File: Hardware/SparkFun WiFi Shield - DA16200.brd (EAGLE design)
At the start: 59.7 x 53.3 mm, 131 parts, among them J1 CORTEX_JTAG_DEBUG, U1 DA16200MOD-AAC4WA32

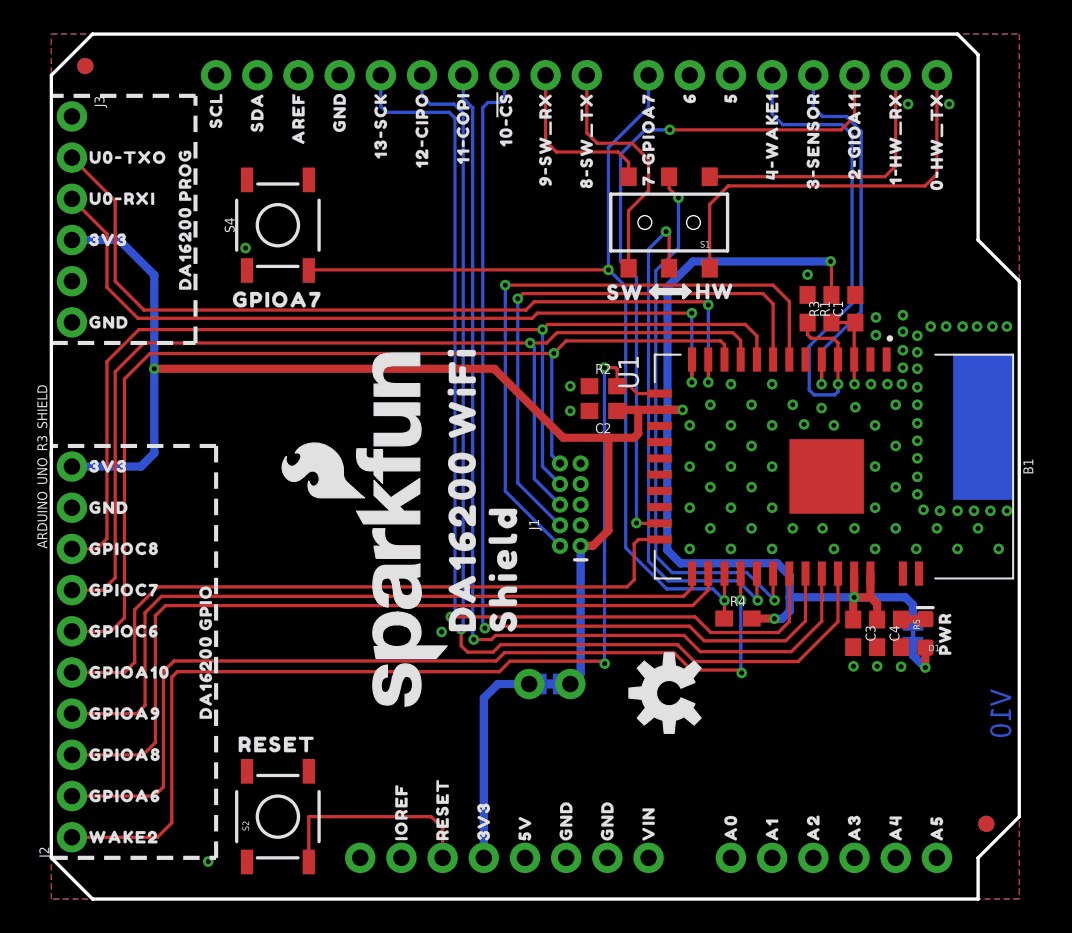
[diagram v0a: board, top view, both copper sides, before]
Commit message: V10 Dialog Changes
- GPIOA6 needs 4.7k Pullup
- GPIOA10 - added 2-way jumper for MCU (SPI Interrupt) and Header (PWM)
- GPIOC6,7,8 not needed for JTAG
- Removed RTC Sensor, RTC_WAKE1, RTC_WAKE2
- PCB - Moved VDD trace, enlarged ground connection for RF GND on bottom, added more vias in large ground areas
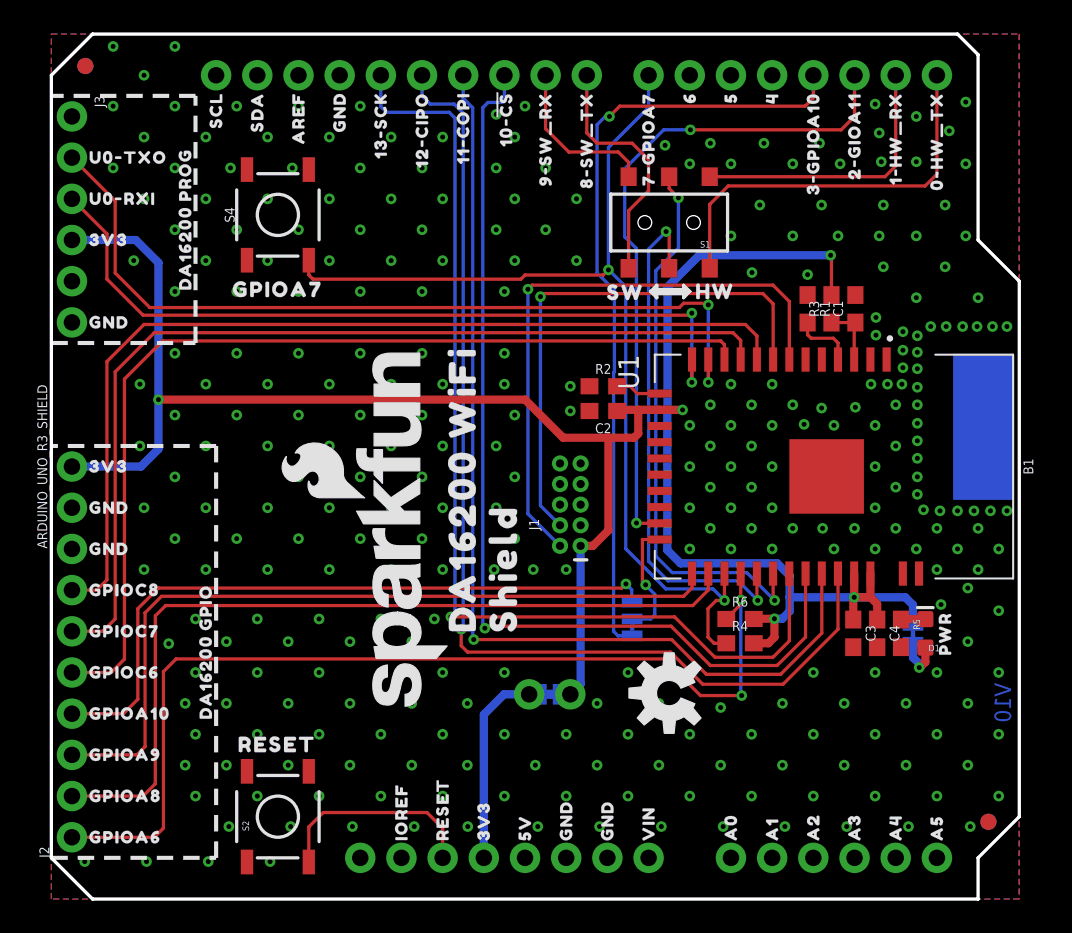
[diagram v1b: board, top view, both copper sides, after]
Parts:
- removed U$69: (no value), output:4#WAKE10
- removed U$96: (no value), output:WAKE20
- added JP2: (no value), SparkFun-Jumpers:SMT-JUMPER_3_1-NC_TRACE_NO-SILK
- added R6: 4.7k, SparkFun-Resistors:0603
- added U$35: (no value), output:GND0
- added U$51: (no value), output:3#GPIOA100
- U$18: device output:4#WAKE10 -> output:40
- U$23: device output:3#SENSOR0 -> output:40
- U$50: device output:WAKE20 -> output:GND0
- U$68: device output:3#SENSOR0 -> output:3#GPIOA100
- moved U$50 17.8 mm to (1.78, 21.6)
- moved U$46 2.54 mm to (1.78, 14.0)
- moved U$47 2.54 mm to (1.78, 11.4)
- moved U$49 2.54 mm to (1.78, 6.35)
- moved U$91 2.54 mm to (1.78, 14.0)
- moved U$92 2.54 mm to (1.78, 11.4)
- moved U$94 2.54 mm to (1.78, 6.35)
- moved U$17 2.54 mm to (1.78, 3.81)
- moved U$95 2.54 mm to (1.78, 3.81)
- moved U$23 2.54 mm to (44.5, 50.3), flipped to the bottom
- moved U$44 2.54 mm to (1.78, 19.1)
- moved U$45 2.54 mm to (1.78, 16.5)
- moved U$48 2.54 mm to (1.78, 8.89)
- moved U$89 2.54 mm to (1.78, 19.1)
- moved U$90 2.54 mm to (1.78, 16.5)
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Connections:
- removed net GPIOA6: J2.2, U1.27
- removed net GPIOA8: J2.3, U1.25
- removed net GPIOA9: J2.4, U1.24
- removed net GPIOC6: J1.10, J2.6, U1.11
- removed net GPIOC7: J1.6, J2.7, U1.10
- removed net GPIOC8: J1.8, J2.8, U1.9
- removed net RTC_SENSOR: B1.D3, U1.5
- removed net RTC_WAKE2: J2.1, R2.2, U1.14
- new net ARD_GPIOA10: B1.D3, JP2.3
- new net HEADER_GPIOA10: J2.4, JP2.1
- new net HEADER_GPIOA6: J2.1, R6.1, U1.27
- new net HEADER_GPIOA8: J2.2, U1.25
- new net HEADER_GPIOA9: J2.3, U1.24
- new net HEADER_GPIOC6: J2.5, U1.11
- new net HEADER_GPIOC7: J2.6, U1.10
- new net HEADER_GPIOC8: J2.7, U1.9
- new net HEADER_RTC_WAKE2: R2.2, U1.14
- net 3.3V: now also R6.2
- net GND: now also J2.8
- net GPIOA10: now also JP2.2; no longer J2.5
- net RTC_WAKE1: no longer B1.D4
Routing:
- net GPIOC7: track 67.4 -> 0.00 mm, vias 1 -> 0
- net GPIOC8: track 66.1 -> 0.00 mm, vias 1 -> 0
- net RTC_WAKE2: track 65.6 -> 0.00 mm, vias 2 -> 0
- net GPIOC6: track 64.4 -> 0.00 mm, vias 1 -> 0
- net HEADER_GPIOA6: track 0.00 -> 61.6 mm, vias 0 -> 2
- net HEADER_GPIOC6: track 0.00 -> 59.8 mm
- net HEADER_GPIOC7: track 0.00 -> 59.2 mm
- net HEADER_GPIOC8: track 0.00 -> 58.7 mm
- net GPIOA6: track 55.8 -> 0.00 mm, vias 2 -> 0
- net HEADER_GPIOA8: track 0.00 -> 51.6 mm
- net GPIOA8: track 49.0 -> 0.00 mm
- net ARD_GPIOA10: track 0.00 -> 48.4 mm, vias 0 -> 1
- net HEADER_GPIOA9: track 0.00 -> 48.2 mm
- net GPIOA9: track 45.7 -> 0.00 mm
- net HEADER_GPIOA10: track 0.00 -> 42.0 mm, vias 0 -> 1
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
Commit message: Parts Update
Updated library for module, added 470k resistor, updated symbols, added jumper notes
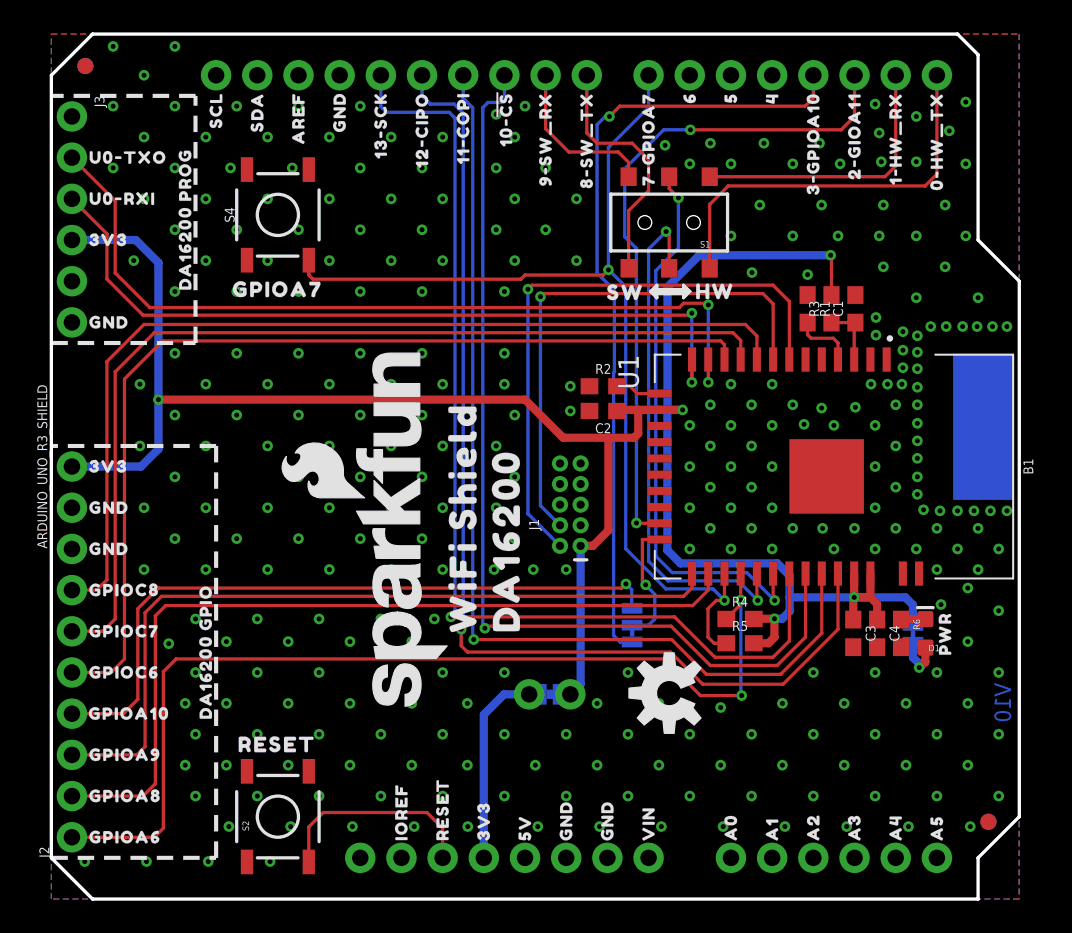
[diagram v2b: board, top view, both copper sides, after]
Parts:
- removed U$102: (no value), output:DA16200_WIFI0
- removed U$103: (no value), output:SHIELD0
- added U$106: (no value), output:HEADER0
- added U$107: (no value), output:WIFI_SHIELD0
- added U$108: (no value), output:DA162000
- added U$69: (no value), output:GPIOA100
- added U$96: (no value), output:D30
- C1: value 1.0uF -> 1uF
- JP2: device SparkFun-Jumpers:SMT-JUMPER_3_1-NC_TRACE_NO-SILK -> SparkFun-Jumpers:SMT-JUMPER_3_1-NC_TRACE_SILK
- R5: value 200 -> 4.7k
- R6: value 4.7k -> 200
- S1: device SparkFun-Electromechanical:AYZ0202 -> SparkFun-Switches:SWITCH_DPDT_SMD_AYZ0202
- U$100: device output:DA16200_WIFI0 -> output:WIFI_SHIELD0
- U$101: device output:SHIELD0 -> output:DA162000
- U1: value DA16200MOD-AAC4WA32 -> DA16200MOD; device DA16200MOD-AAC4WA32:XCVR_DA16200MOD-AAC4WA32 -> DA16200MOD:XCVR_DA16200MOD-AAC4WA32
- moved U$101 27.5 mm to (14.0, 38.2), flipped to the bottom, turned to 180 degrees
- moved U$100 23.9 mm to (14.0, 35.6), flipped to the bottom, turned to 180 degrees
- moved R6 9.97 mm to (52.4, 16.4), turned to 270 degrees
- moved R5 9.95 mm to (42.5, 15.8), turned to 0 degrees
- moved U$47 6.10 mm to (7.87, 11.4)
- moved U$92 6.10 mm to (7.87, 11.4)
- moved R4 1.50 mm to (42.5, 17.3)
- moved JP2 0.38 mm to (35.8, 16.9)
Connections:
- net 3.3V: now also R5.2; no longer R6.2
- net GND: now also R6.2; no longer R5.2
- net GPIOA7: now also R5.1; no longer R4.1
- net HEADER_GPIOA6: now also R4.1; no longer R6.1
- net N$5: now also R6.1; no longer R5.1

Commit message: Added I2C
Added I2C connections, Qwiic connector, pullup resistors, and jumper
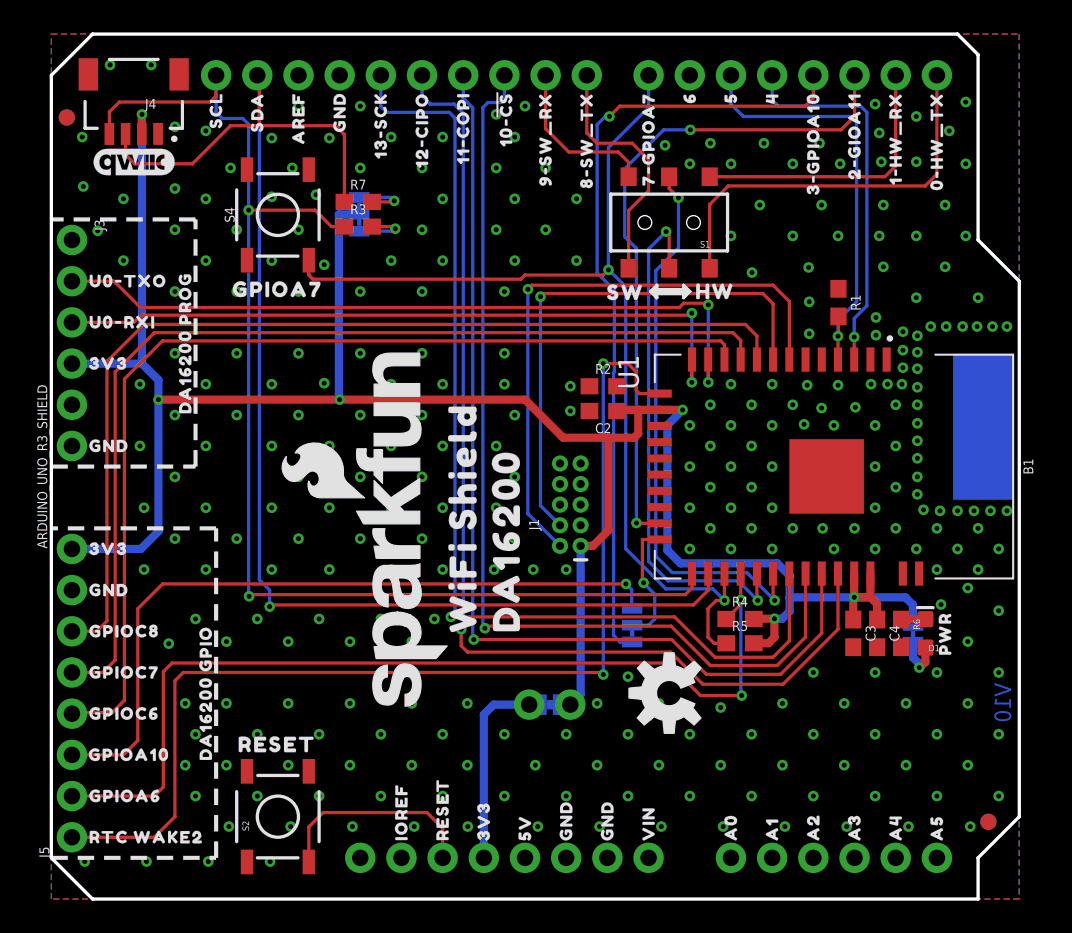
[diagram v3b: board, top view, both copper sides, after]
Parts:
- removed C1: 1uF, SparkFun-Capacitors:0603
- removed J2: (no value), SparkFun-Connectors:1X10_NO_SILK
- removed U$50: (no value), output:GND0
- removed U$93: (no value), output:GPIOA90
- removed U$94: (no value), output:GPIOA80
- added J4: QWIIC_RIGHT_ANGLE, SparkFun-Connectors:JST04_1MM_RA
- added J5: (no value), SparkFun-Connectors:1X08_NO_SILK
- added JP3: (no value), SparkFun-Jumpers:SMT-JUMPER_3_2-NC_TRACE_SILK
- added LOGO4: QWIIC_LOGO_5MM, SparkFun-Aesthetics:QWIIC_5MM
- added R7: 4.7k, SparkFun-Resistors:0603
- R3: value 470k -> 4.7k
- U$35: device output:GND0 -> output:RTC_WAKE20
- U$48: device output:GPIOA90 -> output:RTC_WAKE20
- U$49: device output:GPIOA80 -> output:#I2C#0
- moved U$49 39.0 mm to (17.3, 42.2), flipped to the bottom, turned to 90 degrees
- moved R3 29.6 mm to (18.9, 41.5), turned to 0 degrees
- moved U$35 17.8 mm to (1.78, 3.81), flipped to the top, turned to 0 degrees
- moved U$52 7.62 mm to (1.78, 27.9)
- moved U$86 7.62 mm to (1.78, 27.9)
- moved J3 7.62 mm to (1.27, 40.6)
- moved U$105 7.62 mm to (8.26, 34.3)
- moved U$37 7.62 mm to (1.78, 33.0)
- moved U$53 7.62 mm to (1.78, 38.1)
- moved U$54 7.62 mm to (1.78, 35.6)
- moved U$83 7.62 mm to (1.78, 38.1)
- moved U$84 7.62 mm to (1.78, 35.6)
- moved U$85 7.62 mm to (1.78, 33.0)
- moved U$41 5.08 mm to (1.78, 21.6)
- moved U$87 5.08 mm to (1.78, 21.6)
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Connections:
- removed net HEADER_GPIOA8: J2.2, U1.25
- removed net HEADER_GPIOA9: J2.3, U1.24
- new net ARD_SCL: B1.SCL, J4.4, R3.1, U1.24
- new net ARD_SDA: B1.SDA, J4.3, R7.1, U1.25
- new net N$3: JP3.3, R3.2
- new net N$4: JP3.1, R7.2
- net 3.3V: now also J4.2, J5.8, JP3.2; no longer J2.10, R3.2
- net GND: now also J4.1, J5.7; no longer C1.2, J2.8, J2.9
- net HEADER_GPIOA10: now also J5.3; no longer J2.4
- net HEADER_GPIOA6: now also J5.2; no longer J2.1
- net HEADER_GPIOC6: now also J5.4; no longer J2.5
- net HEADER_GPIOC7: now also J5.5; no longer J2.6
- net HEADER_GPIOC8: now also J5.6; no longer J2.7
- net HEADER_RTC_WAKE2: now also J5.1
- net RTC_PWR_KEY: now also B1.D4; no longer C1.1, R3.1
- net RTC_WAKE1: now also B1.D5
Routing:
- net ARD_SDA: track 0.00 -> 85.2 mm, vias 0 -> 1
- net ARD_SCL: track 0.00 -> 78.1 mm, vias 0 -> 2
- net HEADER_RTC_WAKE2: track 2.81 -> 67.2 mm, vias 0 -> 2
- net HEADER_GPIOA8: track 51.6 -> 0.00 mm
- net HEADER_GPIOA9: track 48.2 -> 0.00 mm
- net RTC_WAKE1: track 3.86 -> 26.3 mm, vias 0 -> 1
- net RTC_PWR_KEY: track 3.82 -> 23.2 mm, vias 0 -> 1
- net 3.3V: track 139.2 -> 145.4 mm, vias 5 -> 6
- net U0TXO: track 52.0 -> 46.3 mm
- net U0RXI: track 48.6 -> 44.1 mm
- net N$3: track 0.00 -> 3.77 mm, vias 0 -> 1
- net N$4: track 0.00 -> 3.65 mm, vias 0 -> 1
- net HEADER_GPIOA6: track 61.6 -> 58.8 mm
- net HEADER_GPIOC6: track 59.8 -> 62.4 mm
- net HEADER_GPIOC8: track 58.7 -> 61.2 mm
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
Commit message: V10 Design Review Changes
Updated label positions, added notes to sch
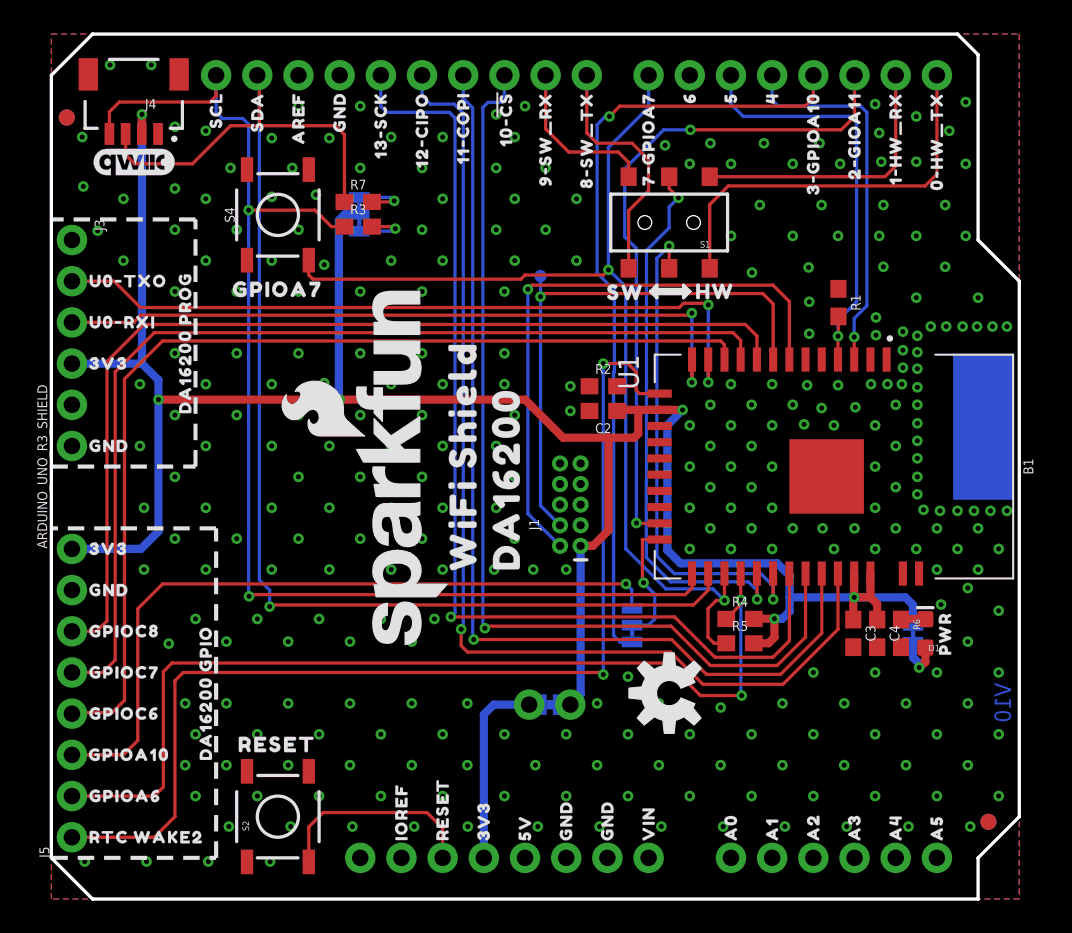
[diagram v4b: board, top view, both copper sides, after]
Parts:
- added TP1: (no value), SparkFun-Connectors:PAD.03X.03
- J4: value QWIIC_RIGHT_ANGLE -> QWIIC_RA
- moved LOGO3 7.73 mm to (19.1, 24.1)
- moved U$100 7.62 mm to (14.0, 27.9)
- moved U$101 7.62 mm to (14.0, 30.6)
- moved LOGO1 3.81 mm to (21.6, 26.7)
- moved U$107 3.81 mm to (25.4, 19.1)
- moved U$108 3.81 mm to (28.1, 19.1)
- renumbered JP3 to I2C
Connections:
- net TCLK: now also TP1.1
- net U1RXI: now also U1.28; no longer U1.29
- net U1TXO: now also U1.29; no longer U1.28
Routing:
- net U1TXO: track 32.6 -> 31.2 mm
- net TCLK: track 32.7 -> 34.0 mm

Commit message: Final Feedback Changes
Changed R3 footprint to locking
Added DNP Capacitor and Resistor
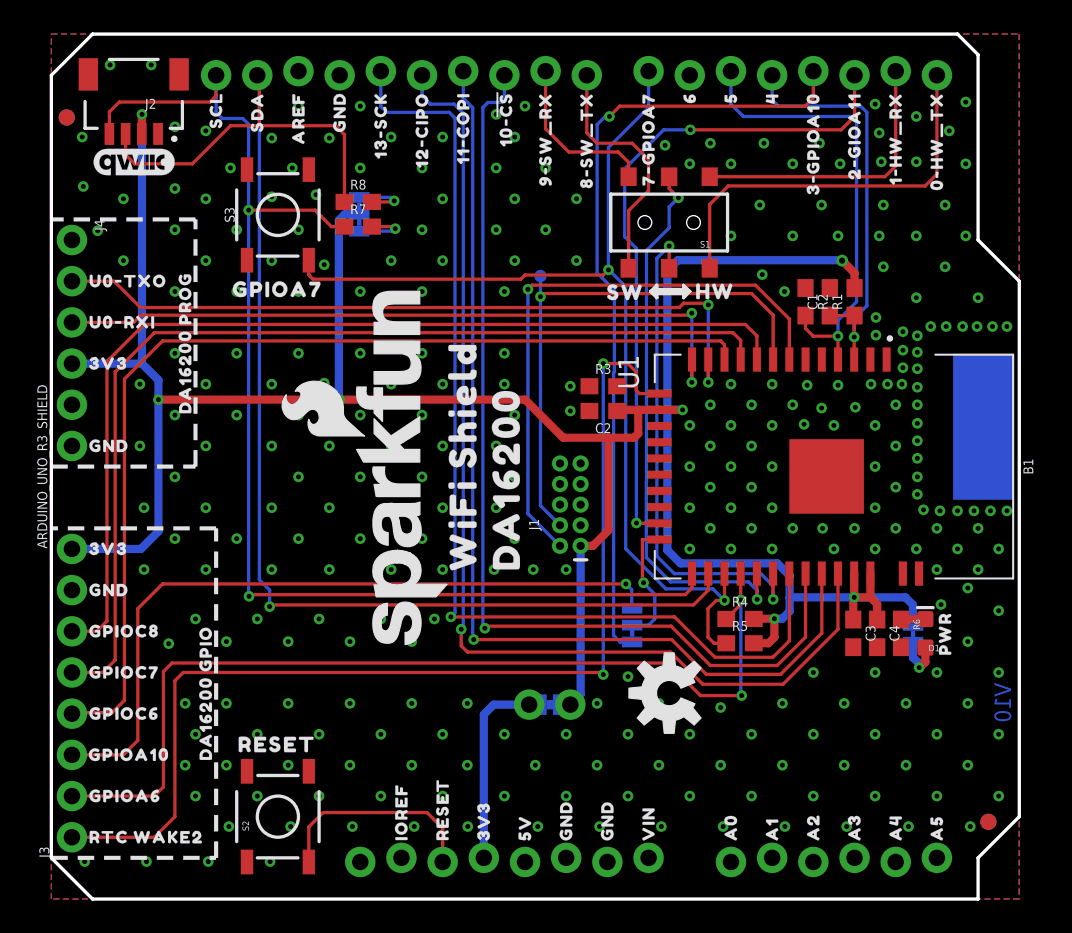
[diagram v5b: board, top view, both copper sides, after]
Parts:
- removed J5: (no value), SparkFun-Connectors:1X08_NO_SILK
- added C1: DNP, SparkFun-Capacitors:0603
- added J2: QWIIC_RA, SparkFun-Connectors:JST04_1MM_RA
- added R8: 4.7k, SparkFun-Resistors:0603
- B1: device SparkFun-Boards:UNO_R3_SHIELD_NOLABELS -> SparkFun-Boards:UNO_R3_SHIELD_NOLABELS_LOCK
- J3: device SparkFun-Connectors:1X06_NO_SILK -> SparkFun-Connectors:1X08_NO_SILK
- J4: value QWIIC_RA -> (none); device SparkFun-Connectors:JST04_1MM_RA -> SparkFun-Connectors:1X06_NO_SILK
- R1: value 4.7k -> DNP
- moved J3 36.8 mm to (1.27, 3.81), turned to 90 degrees
- moved R3 18.0 mm to (34.0, 31.6)
- moved R2 13.5 mm to (46.5, 36.8), turned to 270 degrees
- moved J4 7.57 mm to (1.27, 40.6), turned to 270 degrees
- moved R7 1.52 mm to (18.9, 41.5)
- moved R1 0.99 mm to (49.5, 36.8), turned to 90 degrees
- renumbered S4 to S3
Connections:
- net 3.3V: now also J2.2, J3.8, J4.4, R1.2; no longer J3.4, J4.2, J5.8
- net ARD_SCL: now also J2.4, R7.1; no longer J4.4, R3.1
- net ARD_SDA: now also J2.3, R8.1; no longer J4.3, R7.1
- net GND: now also C1.2, J2.1, J3.7, J4.6, R3.1; no longer J3.6, J4.1, J5.7, R1.1
- net HEADER_GPIOA10: now also J3.3; no longer J5.3
- net HEADER_GPIOA6: now also J3.2; no longer J5.2
- net HEADER_GPIOC6: now also J3.4; no longer J5.4
- net HEADER_GPIOC7: now also J3.5; no longer J5.5
- net HEADER_GPIOC8: now also J3.6; no longer J5.6
- net HEADER_RTC_WAKE2: now also J3.1, R3.2; no longer J5.1, R2.2
- net N$3: now also R7.2; no longer R3.2
- net N$4: now also R8.2; no longer R7.2
- net RTC_PWR_KEY: now also C1.1, R1.1
- net RTC_WAKE1: now also R2.2; no longer R1.2
- net U0RXI: now also J4.3; no longer J3.3
- net U0TXO: now also J4.2; no longer J3.2
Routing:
- net 3.3V: track 145.2 -> 167.4 mm, vias 6 -> 7
- net RTC_PWR_KEY: track 23.2 -> 26.1 mm
- net RTC_WAKE1: track 26.3 -> 28.3 mm
- net TMS: track 36.9 -> 36.2 mm
